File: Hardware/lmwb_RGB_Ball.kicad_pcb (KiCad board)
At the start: 2 copper layers, 65 x 65 mm, 41 parts, among them J1 Conn_01x03, J2 Conn_01x03, U1 AMS1117-3.3, U2 24C02S, U3 STM32C011F6P6

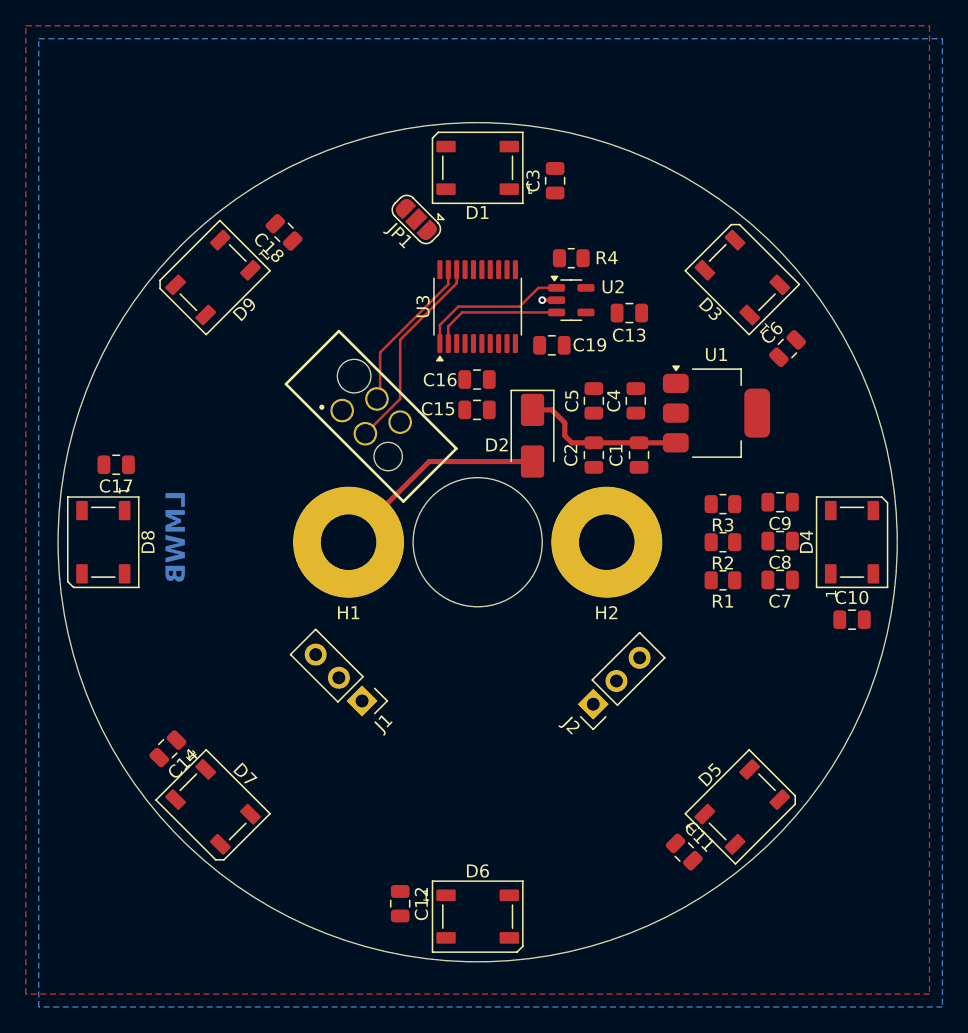
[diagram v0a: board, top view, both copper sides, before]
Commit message: added F04xx project, coded firmware, progress on layout
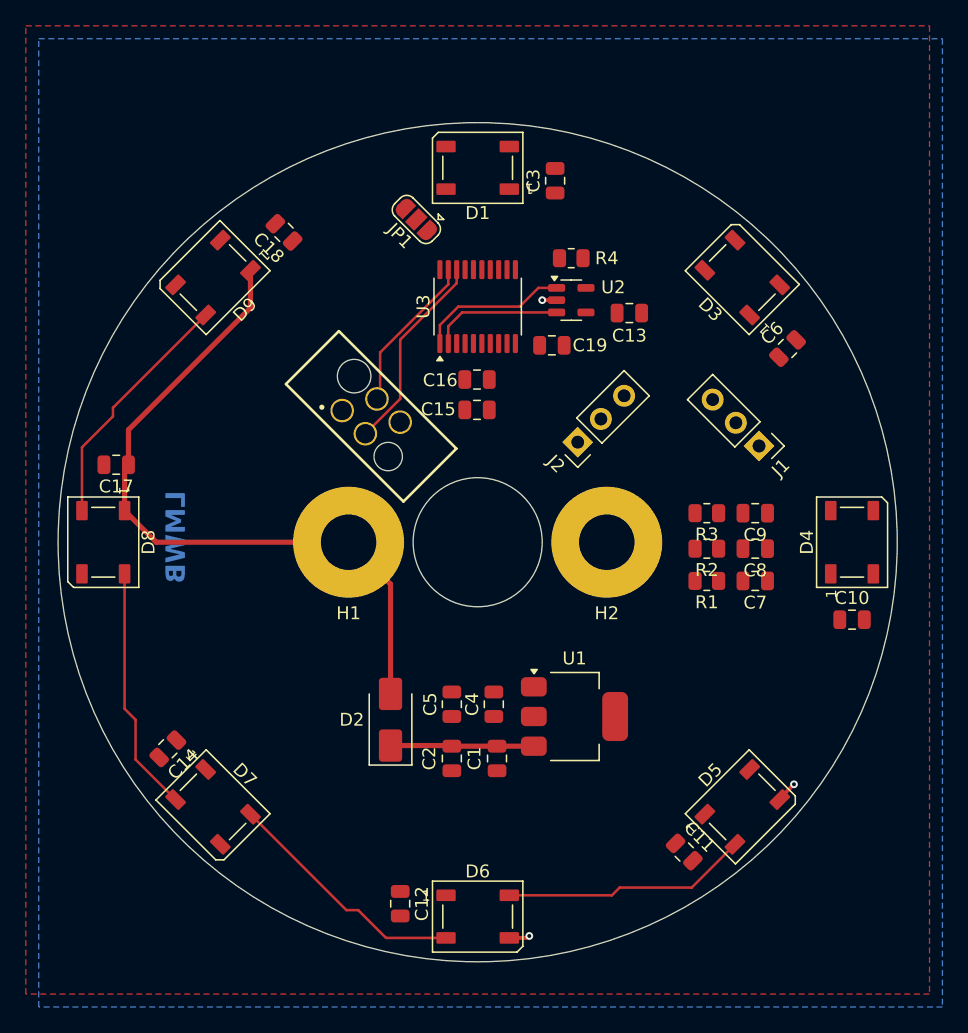
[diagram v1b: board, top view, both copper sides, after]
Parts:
- moved J1 36.5 mm to (91.8, 62.5)
- moved C1 25.9 mm to (71.5, 86.8)
- moved C2 25.9 mm to (68.0, 86.8)
- moved U1 25.9 mm to (77.5, 83.5)
- moved C4 25.9 mm to (71.2, 82.6)
- moved C5 25.9 mm to (68.0, 82.6)
- moved D2 24.6 mm to (63.2, 83.8), turned to 90 degrees
- moved J2 20.3 mm to (77.8, 62.2)
- moved C9 2.11 mm to (91.5, 67.8)
- moved C8 2.02 mm to (91.5, 70.5)
- moved C7 1.93 mm to (91.5, 73.0)
- moved R3 1.43 mm to (87.8, 67.8)
- moved R2 1.35 mm to (87.8, 70.5)
- moved R1 1.25 mm to (87.8, 73.0)
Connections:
- net VCC renamed /Vin
- C10 pad 1: +3V3 -> +5V
- C11 pad 1: +3V3 -> +5V
- C12 pad 1: +3V3 -> +5V
- C14 pad 1: +3V3 -> +5V
- C17 pad 1: +3V3 -> +5V
- C18 pad 1: +3V3 -> +5V
- C3 pad 1: +3V3 -> +5V
- C6 pad 1: +3V3 -> +5V
- C7 pad 1: Net-(J1-Pin_1) -> /EXTI-6
- C8 pad 1: Net-(J1-Pin_2) -> /EXTI-5
- C9 pad 1: Net-(J1-Pin_3) -> /EXTI-4
- D1 pad 1: +3V3 -> +5V
- D2 pad 2: Net-(D2-A) -> +5V
- D3 pad 1: +3V3 -> +5V
- D4 pad 1: +3V3 -> +5V
- D5 pad 1: +3V3 -> +5V
- D6 pad 1: +3V3 -> +5V
- D7 pad 1: +3V3 -> +5V
- D8 pad 1: +3V3 -> +5V
- D9 pad 1: +3V3 -> +5V
- H1 pad 1: Net-(D2-A) -> +5V
- J1 pad 1: Net-(J1-Pin_1) -> /EXTI-6
- J1 pad 2: Net-(J1-Pin_2) -> /EXTI-5
- J1 pad 3: Net-(J1-Pin_3) -> /EXTI-4
- R1 pad 1: Net-(J1-Pin_1) -> /EXTI-6
- R2 pad 1: Net-(J1-Pin_2) -> /EXTI-5
- R3 pad 1: Net-(J1-Pin_3) -> /EXTI-4
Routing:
- net +5V: track 0.00 -> 54.1 mm
- net Net-(D7-DOUT): track 0.00 -> 19.1 mm
- net Net-(D5-DOUT): track 0.00 -> 19.1 mm
- net Net-(D6-DOUT): track 0.00 -> 19.1 mm
- net Net-(D8-DOUT): track 0.00 -> 19.1 mm
- net Net-(D2-A): track 16.8 -> 0.00 mm
- net GND: track 1.11 -> 4.36 mm, vias 1 -> 3
- net /Vin: track 12.7 -> 11.1 mm

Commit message: progress on layout
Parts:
- moved R4 37.6 mm to (49.5, 73.3), turned to 45 degrees
- moved C13 37.4 mm to (54.4, 77.8), turned to -135 degrees
- moved U2 35.2 mm to (51.8, 75.6), turned to 45 degrees
- moved R1 27.5 mm to (75.8, 48.2), turned to 90 degrees
- moved C7 25.9 mm to (75.8, 52.4), turned to -90 degrees
- moved R2 24.3 mm to (78.0, 48.2), turned to 90 degrees
- moved C8 22.6 mm to (78.0, 52.4), turned to -90 degrees
- moved J1 21.3 mm to (80.5, 80.5), turned to 135 degrees
- moved R3 21.0 mm to (80.2, 48.2), turned to 90 degrees
- moved C9 19.1 mm to (80.2, 52.4), turned to -90 degrees
- moved C19 5.57 mm to (72.4, 59.2), turned to -90 degrees
- moved J2 4.03 mm to (78.2, 58.2), turned to 45 degrees
- moved D2 3.95 mm to (60.0, 86.0)
- moved C1 3.74 mm to (68.5, 89.0)
- moved C2 3.74 mm to (65.0, 89.0)
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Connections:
- J2 pad 1: /UART-TX -> /UART-RX
- J2 pad 2: /UART-RX -> /UART-TX
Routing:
- net +5V: track 54.1 -> 190.2 mm, vias 0 -> 2
- net /EXTI-6: track 0.00 -> 49.4 mm, vias 0 -> 3
- net /EXTI-5: track 0.00 -> 47.9 mm, vias 0 -> 3
- net /EXTI-4: track 0.00 -> 46.1 mm, vias 0 -> 3
- net GND: track 4.36 -> 35.7 mm, vias 3 -> 36
- net /SDA: track 10.2 -> 29.5 mm
- net Net-(D3-DOUT): track 0.00 -> 19.1 mm
- net Net-(D4-DOUT): track 0.00 -> 19.1 mm
- net Net-(D1-DOUT): track 0.00 -> 19.1 mm
- net /SCL: track 11.7 -> 29.0 mm
- net /UART-TX: track 0.00 -> 12.2 mm
- net /UART-RX: track 0.00 -> 8.87 mm
- net /SPI-MOSI: track 0.00 -> 5.47 mm
- net /nRST: track 0.00 -> 5.43 mm
- net /SW-CLK: track 12.3 -> 17.1 mm
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- added copper zone on F.Cu, net GND
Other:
- board text added: "TX RX GND"
